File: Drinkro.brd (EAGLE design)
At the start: 75.9 x 55.9 mm, 21 parts, among them J1 POWER_JACKPTH, U1 L293D, U2 L293D

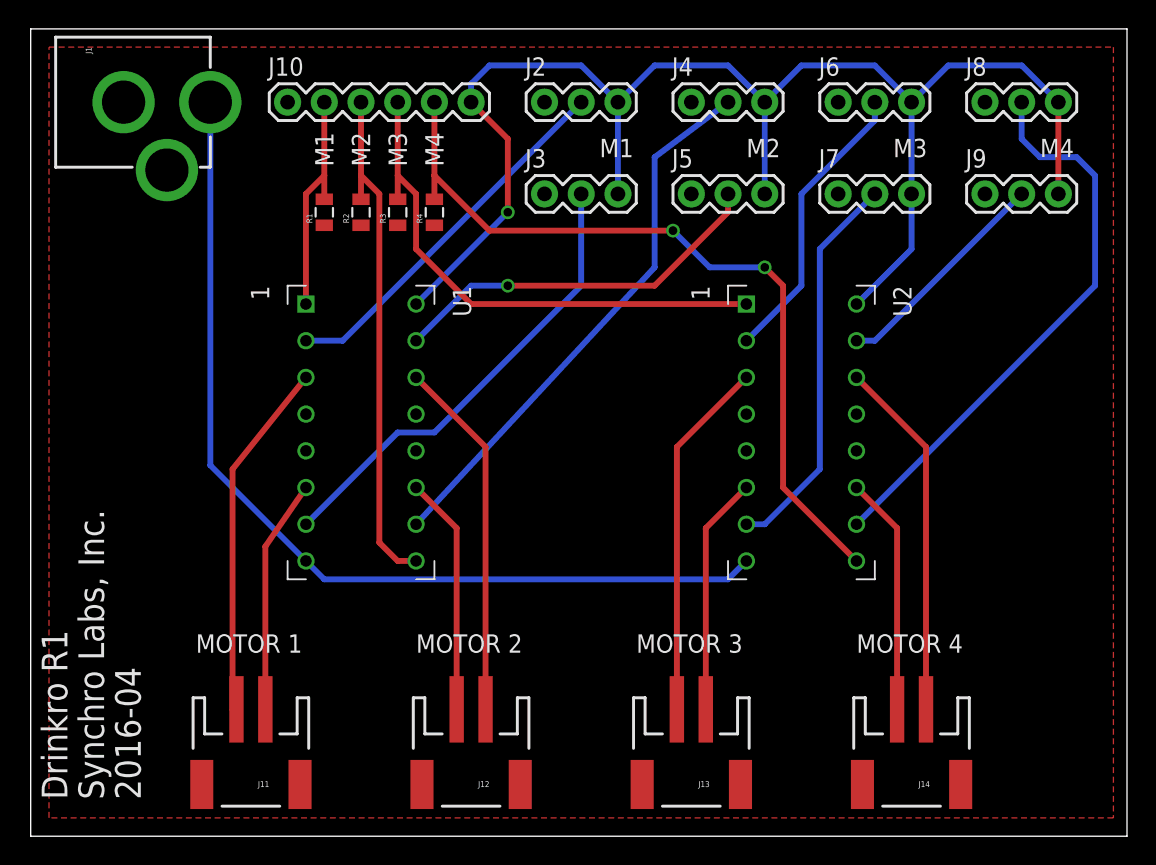
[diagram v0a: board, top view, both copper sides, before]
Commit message: Silkscreen changes. Revision bump to 2.
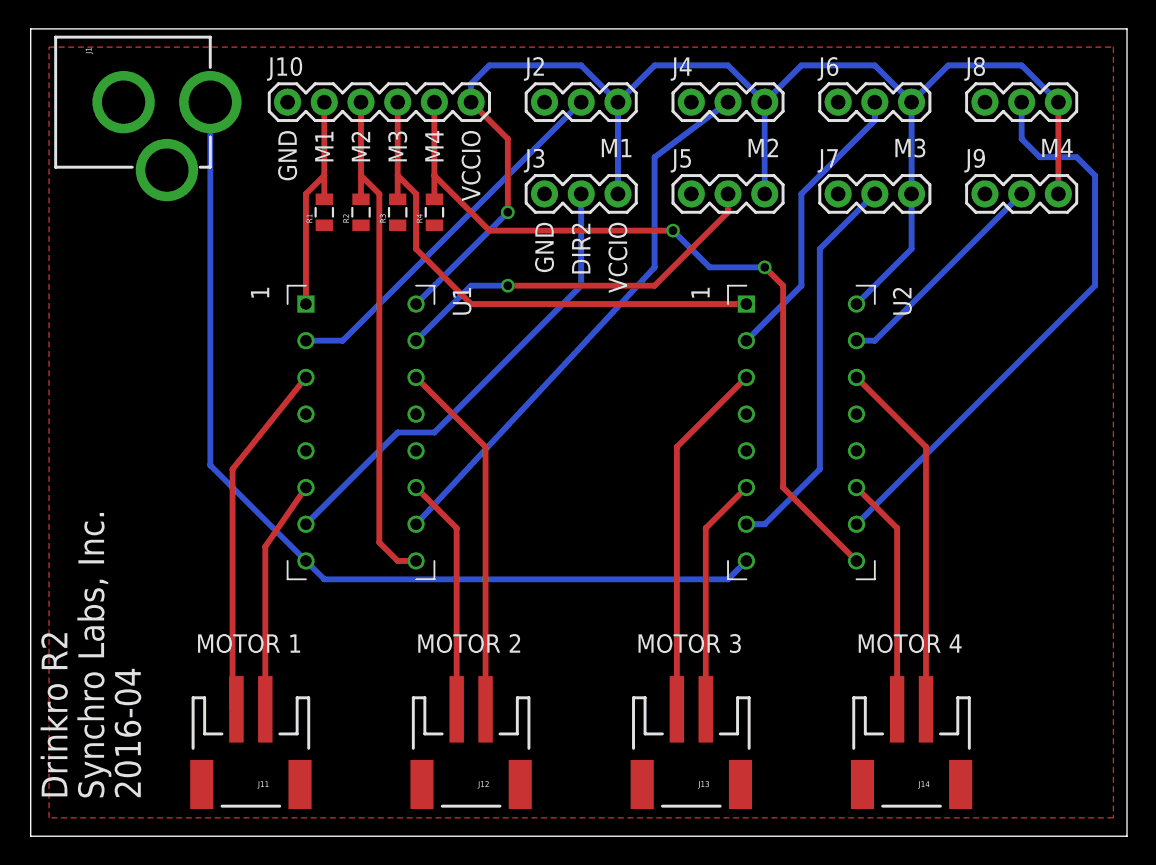
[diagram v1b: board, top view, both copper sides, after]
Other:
- board text added: "DIR2"
- board text added: "Drinkro R2"
- board text added: "GND"
- board text added: "VCCIO"
- board text removed: "Drinkro R1"
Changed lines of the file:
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@@
 <text x="41.91" y="12.7" size="1.27" layer="21">MOTOR 3</text>
 <text x="57.15" y="12.7" size="1.27" layer="21">MOTOR 4</text>
-<text x="20.955" y="46.355" size="1.27" layer="25" rot="R90">M1</text>
-<text x="23.495" y="46.355" size="1.27" layer="25" rot="R90">M2</text>
-<text x="26.035" y="46.355" size="1.27" layer="25" rot="R90">M3</text>
-<text x="28.575" y="46.355" size="1.27" layer="25" rot="R90">M4</text>
+<text x="19.685" y="48.895" size="1.27" layer="25" rot="R90" align="top-right">M1</text>
+<text x="22.225" y="48.895" size="1.27" layer="25" rot="R90" align="top-right">M2</text>
+<text x="24.765" y="48.895" size="1.27" layer="25" rot="R90" align="top-right">M3</text>
+<text x="27.305" y="48.895" size="1.27" layer="25" rot="R90" align="top-right">M4</text>
 <text x="39.37" y="46.99" size="1.27" layer="25">M1</text>
 <text x="49.53" y="46.99" size="1.27" layer="25">M2</text>
 <text x="59.69" y="46.99" size="1.27" layer="25">M3</text>
 <text x="69.85" y="46.99" size="1.27" layer="25">M4</text>
-<text x="2.54" y="2.54" size="1.778" layer="25" rot="R90">Drinkro R1</text>
+<text x="2.54" y="2.54" size="1.778" layer="25" rot="R90">Drinkro R2</text>
 <text x="5.08" y="2.54" size="1.778" layer="25" rot="R90">Synchro Labs, Inc.</text>
 <text x="7.62" y="2.54" size="1.778" layer="25" font="fixed" rot="R90">2016-04</text>
+<text x="29.845" y="48.895" size="1.27" layer="21" rot="R90" align="top-right">VCCIO</text>
+<text x="17.145" y="48.895" size="1.27" layer="21" rot="R90" align="top-right">GND</text>
+<text x="34.925" y="42.545" size="1.27" layer="21" rot="R90" align="top-right">GND</text>
+<text x="40.005" y="42.545" size="1.27" layer="21" rot="R90" align="top-right">VCCIO</text>
+<text x="37.465" y="42.545" size="1.27" layer="21" rot="R90" align="top-right">DIR2</text>
 </plain>
 <attributes>
